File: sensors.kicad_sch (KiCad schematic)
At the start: 9 parts, among them IC4 BME690, U2 BMP581, U3 BME280

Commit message: Assign 0603 footprint to all capacitors
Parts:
- C37, C38, C39, C40, C41, C42: footprint Capacitor_SMD:C_0402_1005Metric_Pad0.74x0.62mm_HandSolder -> Capacitor_SMD:C_0603_1608Metric_Pad1.08x0.95mm_HandSolder
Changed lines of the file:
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@@
 			)
 		)
-		(property "Footprint" "Capacitor_SMD:C_0402_1005Metric_Pad0.74x0.62mm_HandSolder"
+		(property "Footprint" "Capacitor_SMD:C_0603_1608Metric_Pad1.08x0.95mm_HandSolder"
 			(at 210.5152 60.96 0)
 			(effects
@@
 			)
 		)
-		(property "Footprint" "Capacitor_SMD:C_0402_1005Metric_Pad0.74x0.62mm_HandSolder"
+		(property "Footprint" "Capacitor_SMD:C_0603_1608Metric_Pad1.08x0.95mm_HandSolder"
 			(at 82.2452 73.66 0)
 			(effects
@@
 			)
 		)
-		(property "Footprint" "Capacitor_SMD:C_0402_1005Metric_Pad0.74x0.62mm_HandSolder"
+		(property "Footprint" "Capacitor_SMD:C_0603_1608Metric_Pad1.08x0.95mm_HandSolder"
 			(at 100.0252 73.66 0)
 			(effects
@@
 			)
 		)
-		(property "Footprint" "Capacitor_SMD:C_0402_1005Metric_Pad0.74x0.62mm_HandSolder"
+		(property "Footprint" "Capacitor_SMD:C_0603_1608Metric_Pad1.08x0.95mm_HandSolder"
 			(at 83.5152 119.38 0)
 			(effects
@@
 			)
 		)
-		(property "Footprint" "Capacitor_SMD:C_0402_1005Metric_Pad0.74x0.62mm_HandSolder"
+		(property "Footprint" "Capacitor_SMD:C_0603_1608Metric_Pad1.08x0.95mm_HandSolder"
 			(at 97.4852 101.6 0)
 			(effects
@@
 			)
 		)
-		(property "Footprint" "Capacitor_SMD:C_0402_1005Metric_Pad0.74x0.62mm_HandSolder"
+		(property "Footprint" "Capacitor_SMD:C_0603_1608Metric_Pad1.08x0.95mm_HandSolder"
 			(at 171.1452 60.96 0)
 			(effects

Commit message: Fill the cartridge for all schematics
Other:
- company: (none) -> Julien Cruvieux
- title: (none) -> Sensors
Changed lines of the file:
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@@
 	(paper "A4")
 	(title_block
-		(date "2025-11-01")
+		(title "Sensors")
+		(date "2025-12-26")
+		(rev "A")
+		(company "Julien Cruvieux")
 	)
 	(rectangle

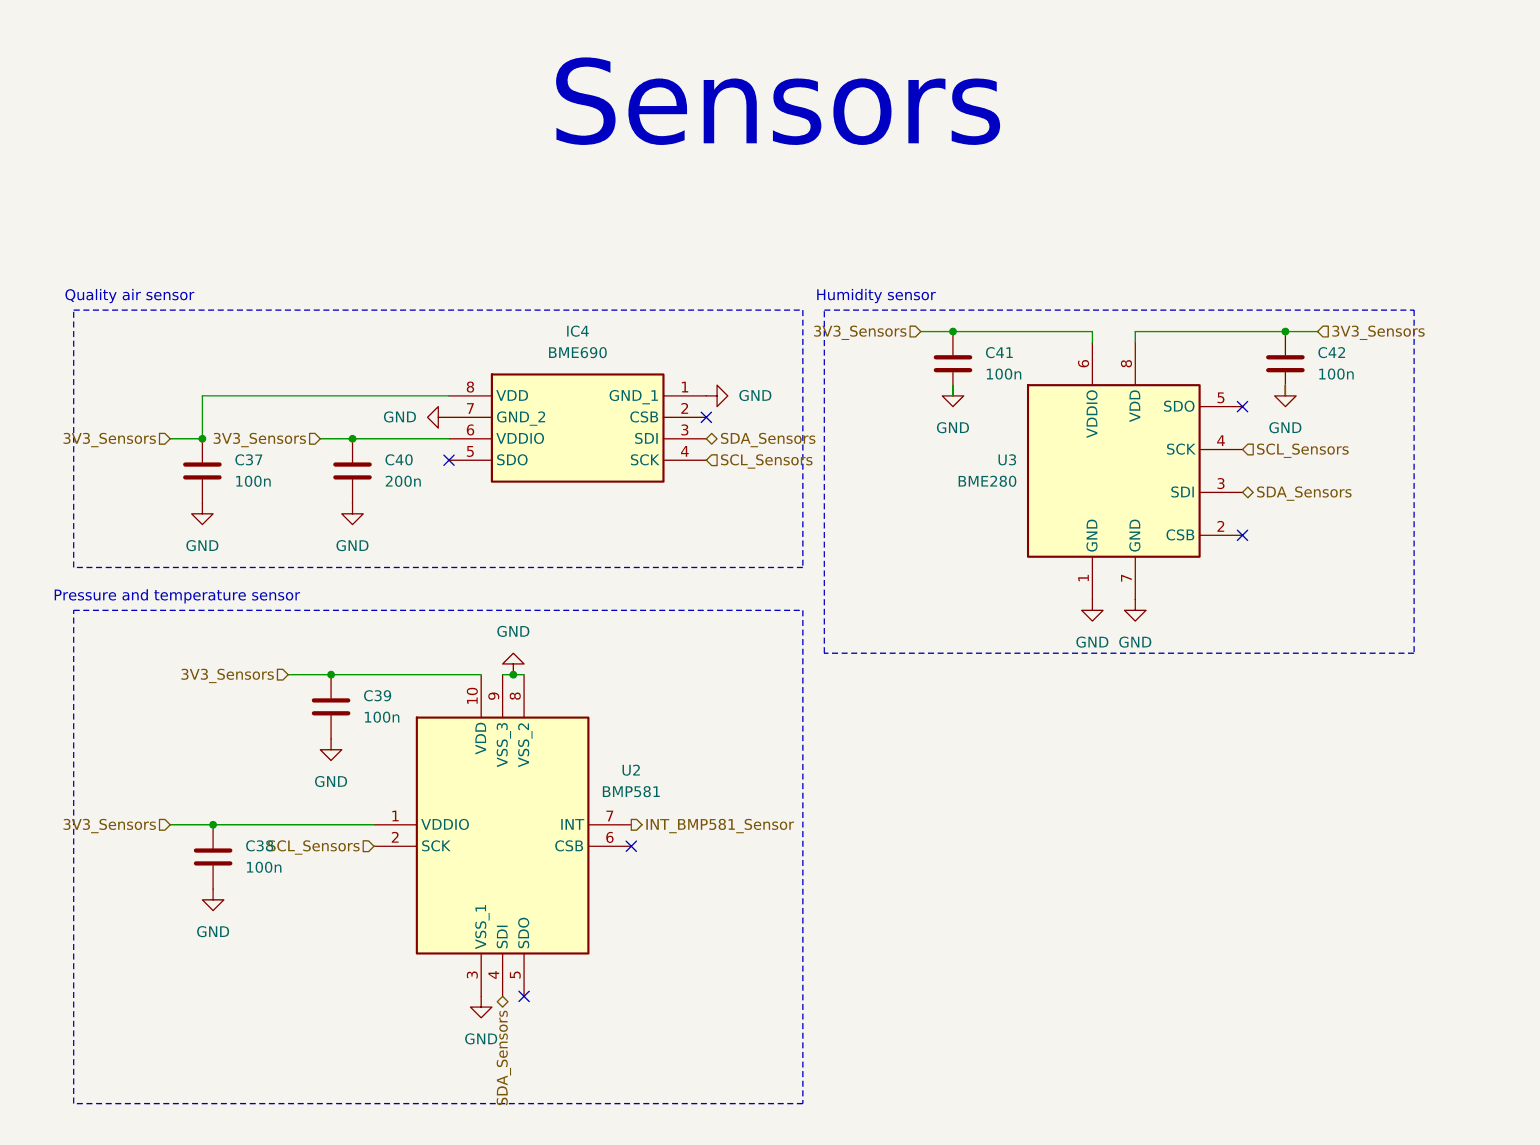
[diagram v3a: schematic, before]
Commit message: Components reindexing and update of PCB
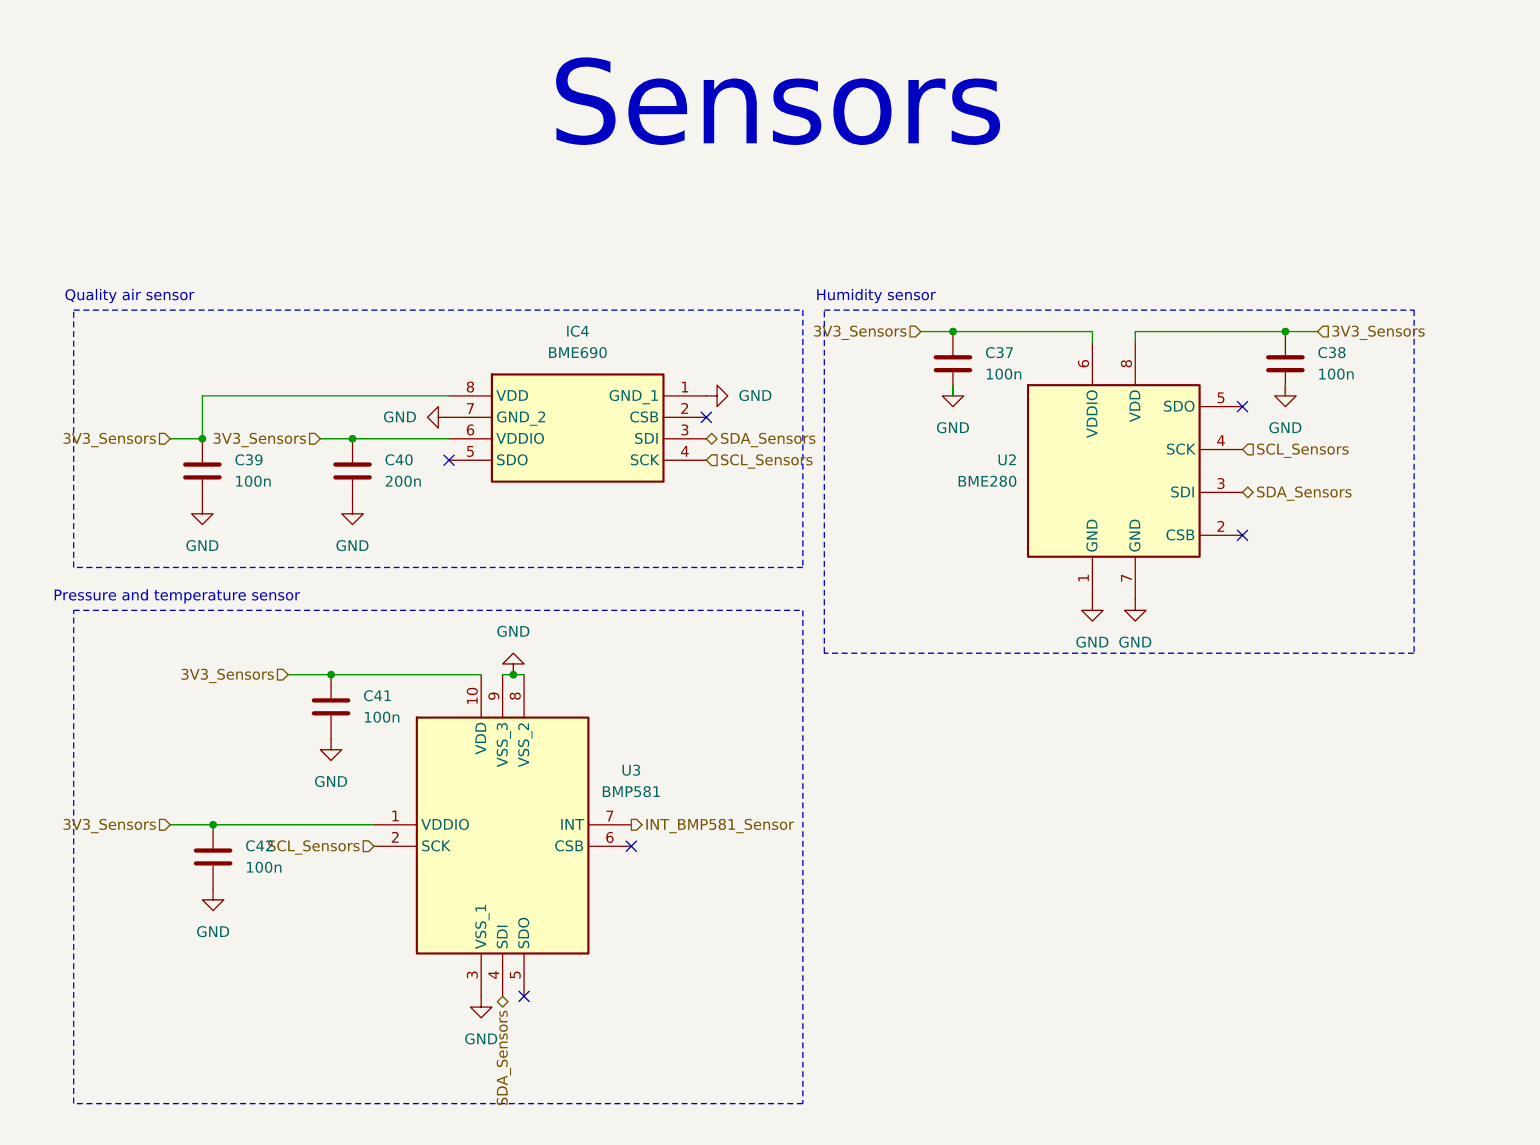
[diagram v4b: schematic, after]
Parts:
- renumbered C41 to C37, C42 to C38, C37 to C39, C39 to C41, C38 to C42, U3 to U2, U2 to U3
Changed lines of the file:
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@@
 		(dnp no)
 		(fields_autoplaced yes)
-		(property "Reference" "#PWR067"
+		(property "Reference" "#PWR059"
 			(at 170.18 66.04 0)
 			(effects
@@
 			(project "weather-station-poc"
 				(path "/38eb53bb-294e-46e4-ad59-fd355ca373b9/29574217-d56b-4a63-a2c4-128dfec2758e"
-					(reference "#PWR067")
+					(reference "#PWR059")
 					(unit 1)
 				)
@@
 		(dnp no)
 		(fields_autoplaced yes)
-		(property "Reference" "#PWR066"
+		(property "Reference" "#PWR061"
 			(at 147.32 60.96 0)
 			(effects
@@
 			(project "weather-station-poc"
 				(path "/38eb53bb-294e-46e4-ad59-fd355ca373b9/29574217-d56b-4a63-a2c4-128dfec2758e"
-					(reference "#PWR066")
+					(reference "#PWR061")
 					(unit 1)
 				)
@@
 		(dnp no)
 		(fields_autoplaced yes)
-		(property "Reference" "C42"
+		(property "Reference" "C38"
 			(at 213.36 55.8799 0)
 			(effects
@@
 			(project "weather-station-poc"
 				(path "/38eb53bb-294e-46e4-ad59-fd355ca373b9/29574217-d56b-4a63-a2c4-128dfec2758e"
-					(reference "C42")
+					(reference "C38")
 					(unit 1)
 				)
@@
 		(dnp no)
 		(fields_autoplaced yes)
-		(property "Reference" "C37"
+		(property "Reference" "C39"
 			(at 85.09 68.5799 0)
 			(effects
@@
 			(project ""
 				(path "/38eb53bb-294e-46e4-ad59-fd355ca373b9/29574217-d56b-4a63-a2c4-128dfec2758e"
-					(reference "C37")
+					(reference "C39")
 					(unit 1)
 				)
@@
 		(dnp no)
 		(fields_autoplaced yes)
-		(property "Reference" "#PWR059"
+		(property "Reference" "#PWR063"
 			(at 81.28 80.01 0)
 			(effects
@@
 			(project ""
 				(path "/38eb53bb-294e-46e4-ad59-fd355ca373b9/29574217-d56b-4a63-a2c4-128dfec2758e"
-					(reference "#PWR059")
+					(reference "#PWR063")
 					(unit 1)
 				)
@@
 		(dnp no)
 		(fields_autoplaced yes)
-		(property "Reference" "#PWR069"
+		(property "Reference" "#PWR066"
 			(at 191.77 91.44 0)
 			(effects
@@
 			(project "weather-station-poc"
 				(path "/38eb53bb-294e-46e4-ad59-fd355ca373b9/29574217-d56b-4a63-a2c4-128dfec2758e"
-					(reference "#PWR069")
+					(reference "#PWR066")
 					(unit 1)
 				)
@@
 		(dnp no)
 		(fields_autoplaced yes)
-		(property "Reference" "#PWR065"
+		(property "Reference" "#PWR067"
 			(at 118.11 87.63 0)
 			(effects
@@
 			(project "weather-station-poc"
 				(path "/38eb53bb-294e-46e4-ad59-fd355ca373b9/29574217-d56b-4a63-a2c4-128dfec2758e"
-					(reference "#PWR065")
+					(reference "#PWR067")
 					(unit 1)
 				)
@@
 		(dnp no)
 		(fields_autoplaced yes)
-		(property "Reference" "#PWR062"
+		(property "Reference" "#PWR064"
 			(at 99.06 80.01 0)
 			(effects
@@
 			(project "weather-station-poc"
 				(path "/38eb53bb-294e-46e4-ad59-fd355ca373b9/29574217-d56b-4a63-a2c4-128dfec2758e"
-					(reference "#PWR062")
+					(reference "#PWR064")
 					(unit 1)
 				)
@@
 		(dnp no)
 		(fields_autoplaced yes)
-		(property "Reference" "#PWR070"
+		(property "Reference" "#PWR060"
 			(at 209.55 66.04 0)
 			(effects
@@
 			(project "weather-station-poc"
 				(path "/38eb53bb-294e-46e4-ad59-fd355ca373b9/29574217-d56b-4a63-a2c4-128dfec2758e"
-					(reference "#PWR070")
+					(reference "#PWR060")
 					(unit 1)
 				)
@@
 		(dnp no)
 		(fields_autoplaced yes)
-		(property "Reference" "U2"
+		(property "Reference" "U3"
 			(at 132.08 105.3398 0)
 			(effects
@@
 			(project "weather-station-poc"
 				(path "/38eb53bb-294e-46e4-ad59-fd355ca373b9/29574217-d56b-4a63-a2c4-128dfec2758e"
-					(reference "U2")
+					(reference "U3")
 					(unit 1)
 				)
@@
 		(dnp no)
 		(fields_autoplaced yes)
-		(property "Reference" "#PWR060"
+		(property "Reference" "#PWR069"
 			(at 82.55 125.73 0)
 			(effects
@@
 			(project "weather-station-poc"
 				(path "/38eb53bb-294e-46e4-ad59-fd355ca373b9/29574217-d56b-4a63-a2c4-128dfec2758e"
-					(reference "#PWR060")
+					(reference "#PWR069")
 					(unit 1)
 				)
@@
 		(dnp no)
 		(fields_autoplaced yes)
-		(property "Reference" "#PWR061"
+		(property "Reference" "#PWR068"
 			(at 96.52 107.95 0)
 			(effects
@@
 			(project "weather-station-poc"
 				(path "/38eb53bb-294e-46e4-ad59-fd355ca373b9/29574217-d56b-4a63-a2c4-128dfec2758e"
-					(reference "#PWR061")
+					(reference "#PWR068")
 					(unit 1)
 				)
@@
 		(dnp no)
 		(fields_autoplaced yes)
-		(property "Reference" "U3"
+		(property "Reference" "U2"
 			(at 177.8 68.5799 0)
 			(effects
@@
 			(project "weather-station-poc"
 				(path "/38eb53bb-294e-46e4-ad59-fd355ca373b9/29574217-d56b-4a63-a2c4-128dfec2758e"
-					(reference "U3")
+					(reference "U2")
 					(unit 1)
 				)
@@
 		(dnp no)
 		(fields_autoplaced yes)
-		(property "Reference" "#PWR064"
+		(property "Reference" "#PWR070"
 			(at 114.3 138.43 0)
 			(effects
@@
 			(project "weather-station-poc"
 				(path "/38eb53bb-294e-46e4-ad59-fd355ca373b9/29574217-d56b-4a63-a2c4-128dfec2758e"
-					(reference "#PWR064")
+					(reference "#PWR070")
 					(unit 1)
 				)
@@
 		(dnp no)
 		(fields_autoplaced yes)
-		(property "Reference" "#PWR063"
+		(property "Reference" "#PWR062"
 			(at 104.14 63.5 0)
 			(effects
@@
 			(project "weather-station-poc"
 				(path "/38eb53bb-294e-46e4-ad59-fd355ca373b9/29574217-d56b-4a63-a2c4-128dfec2758e"
-					(reference "#PWR063")
+					(reference "#PWR062")
 					(unit 1)
 				)
@@
 		(dnp no)
 		(fields_autoplaced yes)
-		(property "Reference" "C38"
+		(property "Reference" "C42"
 			(at 86.36 114.2999 0)
 			(effects
@@
 			(project "weather-station-poc"
 				(path "/38eb53bb-294e-46e4-ad59-fd355ca373b9/29574217-d56b-4a63-a2c4-128dfec2758e"
-					(reference "C38")
+					(reference "C42")
 					(unit 1)
 				)
@@
 		(dnp no)
 		(fields_autoplaced yes)
-		(property "Reference" "#PWR068"
+		(property "Reference" "#PWR065"
 			(at 186.69 91.44 0)
 			(effects
@@
 			(project "weather-station-poc"
 				(path "/38eb53bb-294e-46e4-ad59-fd355ca373b9/29574217-d56b-4a63-a2c4-128dfec2758e"
-					(reference "#PWR068")
+					(reference "#PWR065")
 					(unit 1)
 				)
@@
 		(dnp no)
 		(fields_autoplaced yes)
-		(property "Reference" "C39"
+		(property "Reference" "C41"
 			(at 100.33 96.5199 0)
 			(effects
@@
 			(project "weather-station-poc"
 				(path "/38eb53bb-294e-46e4-ad59-fd355ca373b9/29574217-d56b-4a63-a2c4-128dfec2758e"
-					(reference "C39")
+					(reference "C41")
 					(unit 1)
 				)
@@
 		(dnp no)
 		(fields_autoplaced yes)
-		(property "Reference" "C41"
+		(property "Reference" "C37"
 			(at 173.99 55.8799 0)
 			(effects
@@
 			(project "weather-station-poc"
 				(path "/38eb53bb-294e-46e4-ad59-fd355ca373b9/29574217-d56b-4a63-a2c4-128dfec2758e"
-					(reference "C41")
-					(unit 1)
-				)
+					(reference "C37")
+					(unit 1)
+				)
